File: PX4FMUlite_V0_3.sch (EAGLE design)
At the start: 145 parts, among them J2 DF13-4P-1.25V, J201 DF13C-6P-1.25V, J202 DF13C-6P-1.25V, J203 DF13C-6P-1.25V, J301 47346-0001, J302 DF13C-4P-1.25V, J401 DF13C-4P-1.25V, J403 DF13C-7P-1.25V, J405 DF13C-4P-1.25V, J801 JST-ZH-3, J802 DF13C-3P-1.25V, M3_MOUNT1101 MOUNT-HOLE3.1MM, M3_MOUNT1102 MOUNT-HOLE3.1MM, M3_MOUNT1103 MOUNT-HOLE3.1MM, M3_MOUNT1104 MOUNT-HOLE3.1MM, U1 MPU-6000QFN-24, U101 STM32F4X7VX, U401 MAX3051, U903 74LVC2G240, X101 3.2x2.5 mm / 24 MHz / 15 ppm

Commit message: More tweaks
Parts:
- removed J301: 47346-0001, pixhawk2:MOLEX-47346-0001
- removed R12, R13: 120R, pixhawk2:RESISTOR0402-RES
- removed U$301: NUF2042XV6, pixhawk2:NUF2042XV6
- added C4: 0u1, pixhawk2:CAP0402
- added J3: DF13C-4P-1.25V, con-hirose-df13:DF13-4P-1.25V
- added JP3: JUMPER-3SMD, SparkFun-Passives:JUMPER-3SMD
- added L7: KNH16C104DA5TS, pixhawk2:KNH16C104DA5TS
- added R4: 120R, pixhawk2:RESISTOR0402-RES
- added SJ2: SOLDERJUMPERTRACE, SparkFun-Passives:SOLDERJUMPERTRACE
- added U$5: NUF2042XV6, PX4lite:NUF2042XV6
- added U$7: PESD0402-140, pixhawk2:DIODE-TVS
- added U2: MAX3051, pixhawk2:MAX3051MAX3051EKA
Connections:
- removed net N$14: J203.4, R12.2
- removed net N$19: J203.5, R13.2
- new net N$28: J3.1, L7.P$2, U$7.C
- new net N$29: R4.2, SJ2.1
- new net N$31: JP3.2, L4.P$1
- net CAN2_RX: now also U2.DOUT; no longer R13.1
- net CAN2_TX: now also U2.DIN; no longer R12.1
- net CAN_H: now also J3.2, R4.1, U2.CANH
- net CAN_L: now also J3.3, SJ2.2, U2.CANL
- net FMU-VDD_3V3: now also C4.1, U2.VCC
- net GND: now also L6G$9.GND
- net GNDX: now also C4.2, J3.4, L7.P$3, U$5.GND, U$7.A, U2.GND, U2.RS, U2.SHDN; no longer J301.5, J301.GND1, J301.GND2, J301.GND3, J301.GND4, U$301.GND
- net OTG_DM1: now also U$5.D2I; no longer J301.2, U$301.D1I
- net OTG_DP1: now also U$5.D1I; no longer J301.3, U$301.D2I
- net OTG_FS_DM: now also U$5.D2O; no longer U$301.D1O
- net OTG_FS_DP: now also U$5.D1O; no longer U$301.D2O
- net VBUS: now also U$5.VBUS; no longer J301.1, U$301.VBUS
- net VDD_5V_PERIPH: now also JP3.1, JP3.3, L5.P$1, L7.P$1
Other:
- moved on the sheet: C2, C3, C402, J2, J302, J401, J405, L4, L403, L5, L6G$1, L6G$2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

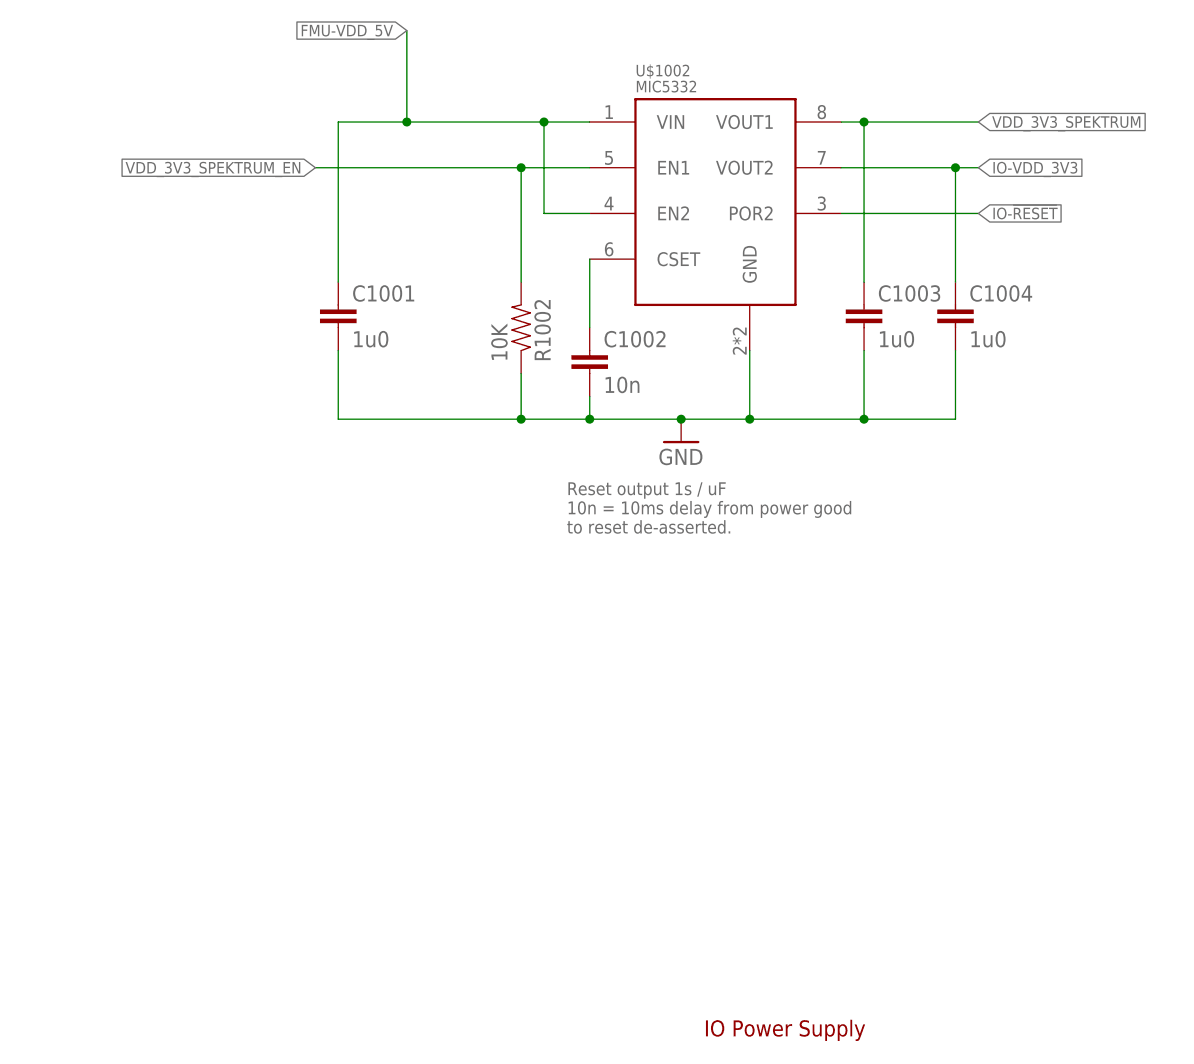
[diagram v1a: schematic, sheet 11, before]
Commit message: Change IO power to 3V3 peripheral power
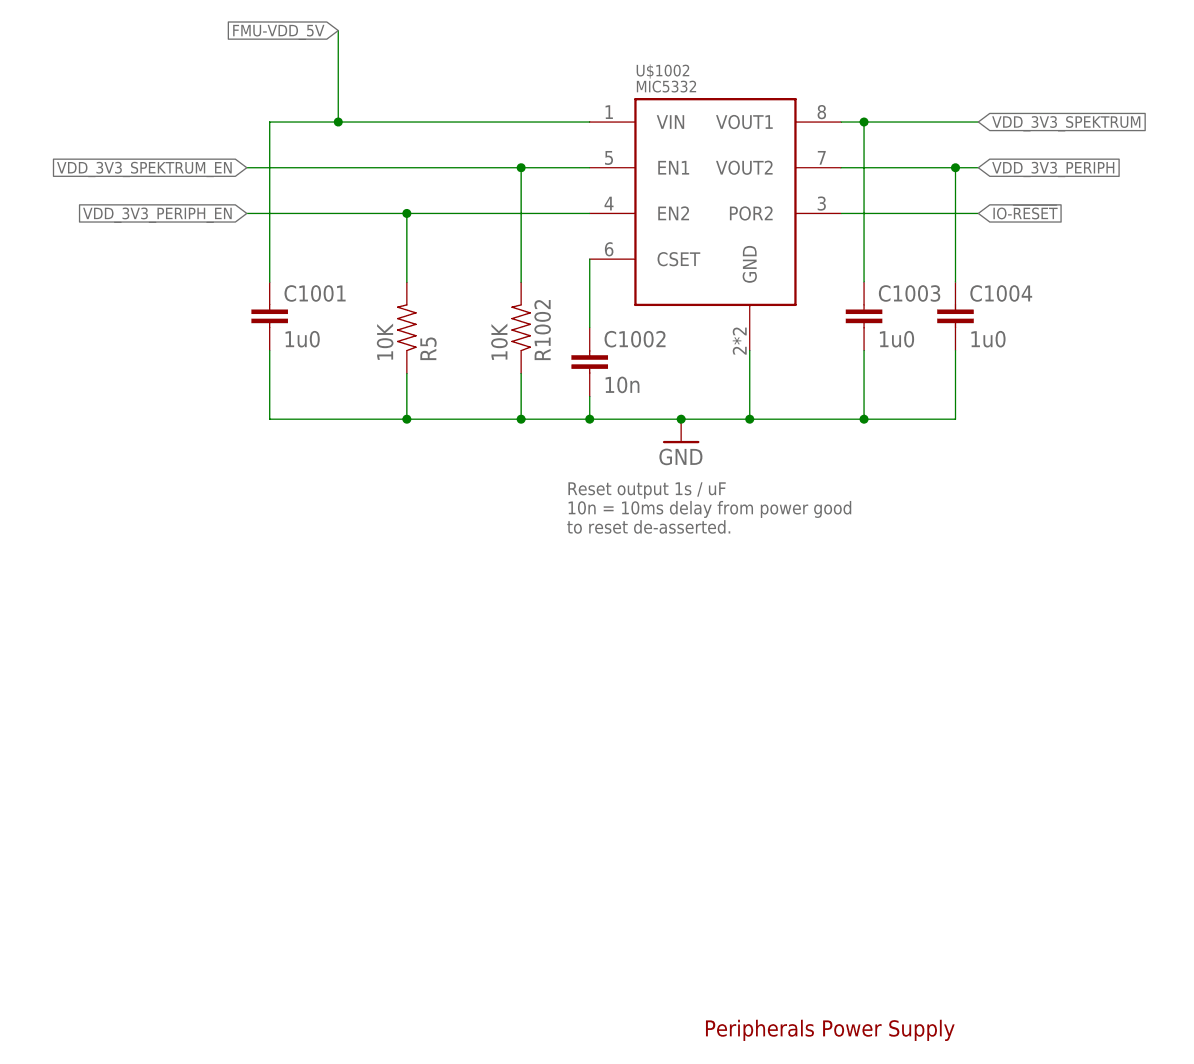
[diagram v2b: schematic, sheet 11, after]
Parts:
- removed ADC_PR, IO-BOOT1101, VDD_5V_BRICK: PAD.04, pixhawk2:PAD.04
- added R5: 10K, pixhawk2:RESISTOR0402-RES
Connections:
- removed net CAN_H: CAN_H.P$1, J3.2, J405.2, R4.1, R409.1, U2.CANH, U401.CANH
- removed net CAN_L: CAN_L.P$1, J3.3, J405.3, SJ1.2, SJ2.2, U2.CANL, U401.CANL
- removed net IO-BOOT0: IO-BOOT1101.P$1
- removed net IO-VDD_3V3: C1004.1, C901.1, U$1002.VOUT2, U903.VCC
- removed net PRESSURE_SENS_IN: ADC_PR.P$1
- removed net VDD_5V_BRICK: VDD_5V_BRICK.P$1
- new net CAN1_H: CAN_H.P$1, J405.2, R409.1, U401.CANH
- new net CAN1_L: CAN_L.P$1, J405.3, SJ1.2, U401.CANL
- new net CAN2_H: J3.2, R4.1, U2.CANH
- new net CAN2_L: J3.3, SJ2.2, U2.CANL
- new net VDD_3V3_PERIPH: C1004.1, C901.1, JP3.1, U$1002.VOUT2, U903.VCC
- new net VDD_3V3_PERIPH_EN: R5.2, U$1002.EN2
- net FMU-BOOT0: no longer FMU-BOOT1101.P$1
- net FMU-VDD_5V: no longer U$1002.EN2
- net GNDX: now also R5.1
- net VDD_5V_PERIPH: no longer JP3.1
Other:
- note added: "Peripherals Power Supply"
- note removed: "IO Power Supply"
- moved on the sheet: C1001

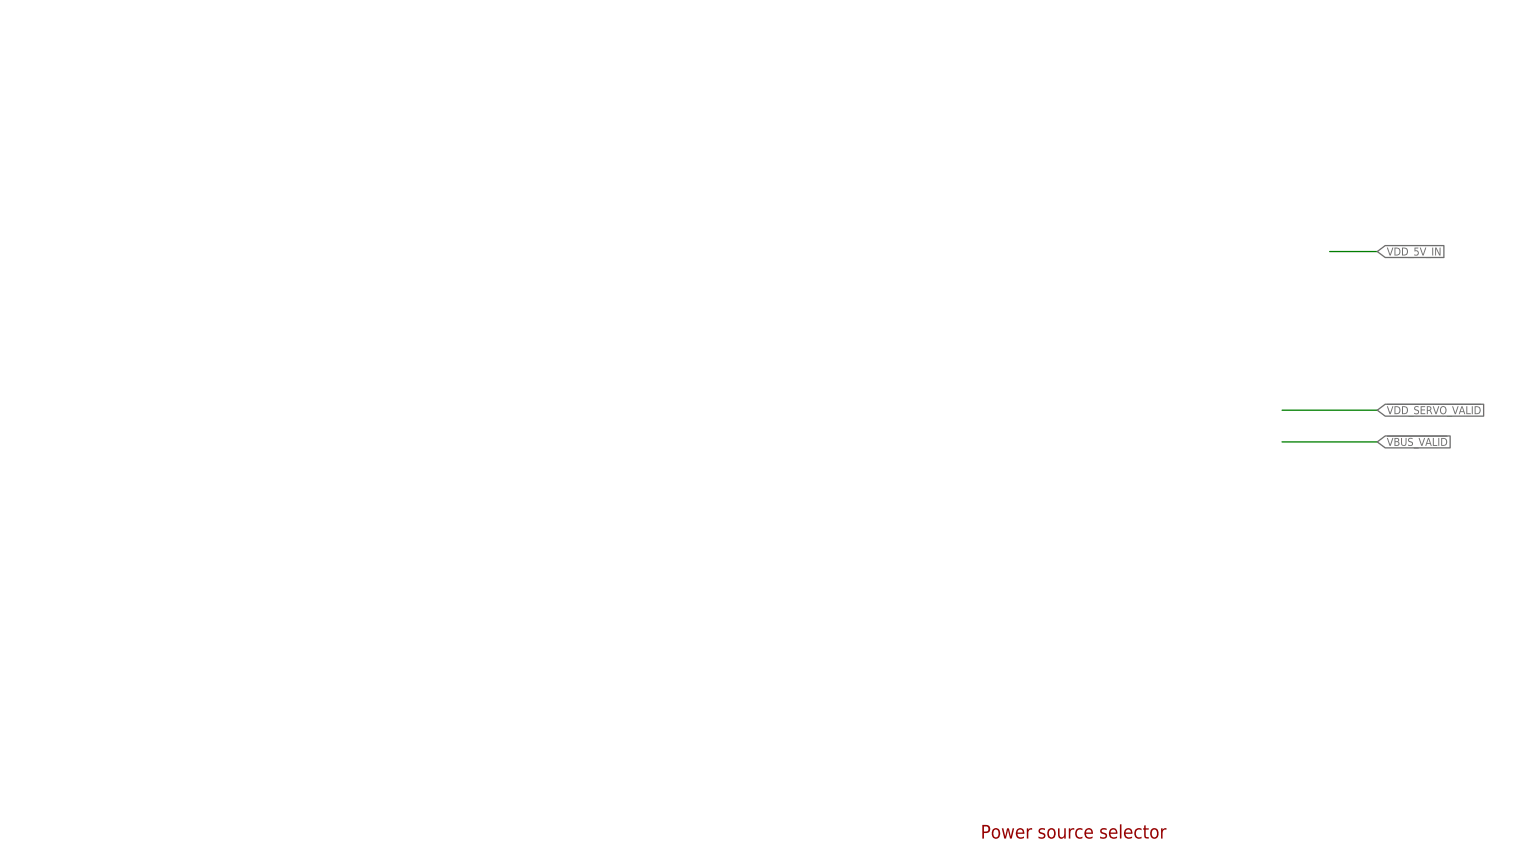
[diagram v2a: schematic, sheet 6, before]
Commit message: Added TPS62143 buck, moved mounting points
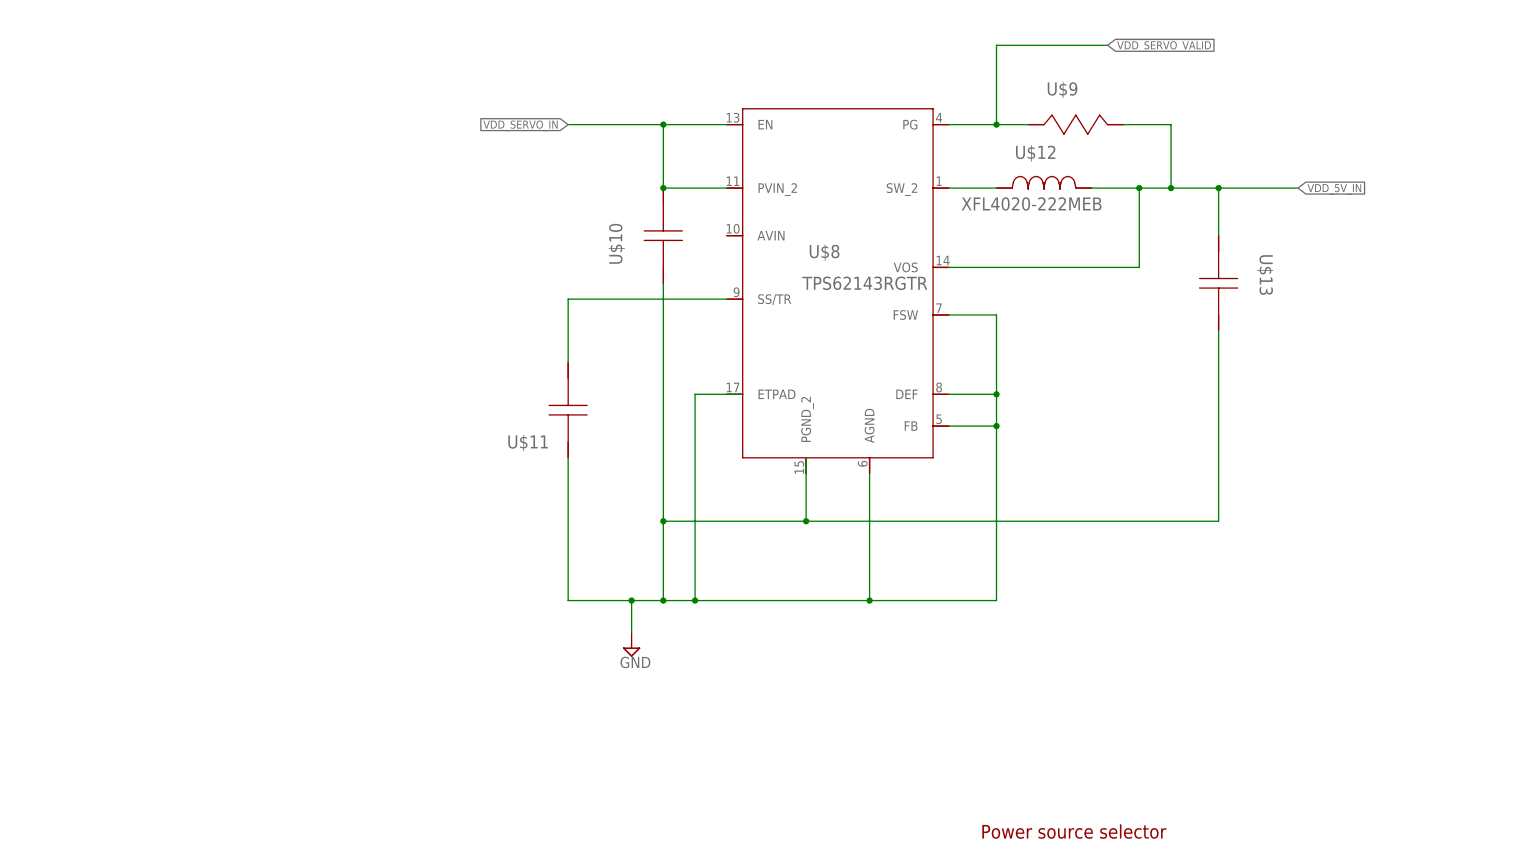
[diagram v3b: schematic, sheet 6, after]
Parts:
- added U$10: GRM21BR61C106KE15L, ti_tps_soln2:GRM21BR61C106KE15L
- added U$11: GRM155R61C223KA01D, ti_tps_soln2:GRM155R61C223KA01D
- added U$12: XFL4020-222MEB, ti_tps_soln2:XFL4020-222MEB
- added U$13: LMK212BJ226MG-T, ti_tps_soln2:LMK212BJ226MG-T
- added U$8: TPS62143RGTR, ti_tps_soln2:TPS62143RGTR
- added U$9: CRCW0402100KFKED, ti_tps_soln2:CRCW0402100KFKED
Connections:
- new net N$14: U$12.2, U$8.SW_2
- new net N$40: U$11.1, U$8.SS/TR
- net !VDD_SERVO_VALID: now also U$8.PG, U$9.2
- net GND: now also U$10.2, U$11.2, U$13.1, U$8.AGND, U$8.DEF, U$8.ETPAD, U$8.FB, U$8.FSW, U$8.PGND_2
- net VDD_5V_IN: now also U$12.1, U$13.2, U$8.VOS, U$9.1
- net VDD_SERVO_IN: now also U$10.1, U$8.EN, U$8.PVIN_2
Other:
- moved on the sheet: JX301-GND1, JX301-GND2, JX301-GND3, JX301-TCK/SWCLK, JX301-TDI/EXTB, JX301-TDO/SWO, JX301-TMS/SWDIO, JX301-VTREF, JX301-~{RESET}

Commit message: Changed to MAX21100
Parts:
- removed C1: 10n, pixhawk2:CAP0402
- removed C507: 0u1, pixhawk2:CAP0402
- removed C509: 10u/10V, pixhawk2:CAP0805
- removed C510: 0u47, pixhawk2:CAP0402
- removed S4RX, S4TX, S5_RX, S5_TX: PAD.04, pixhawk2:PAD.04
- removed U1: MPU-6000QFN-24, SparkFun-Sensors:MPU-6000QFN-24
- added C5: 0u1, pixhawk2:CAP0402
- U$2: value LSM303D -> MAX21100; device PX4FMUlite_V0_1:LSM303D -> PX4lite:MAX21100
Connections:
- removed net N$10: C510.1, U$2.SETC
- removed net N$17: C510.2, U$2.SETP
- removed net N$25: C505.1, U1.CPOUT
- removed net N$27: C1.1, U1.REGOUT
- removed net N$6: C509.1, U$2.C1
- removed net SERIAL4_RX: L3G$3.P$2, S4RX.P$1
- removed net SERIAL4_TX: L3G$4.P$2, S4TX.P$1
- removed net SERIAL5_RX: L3G$1.P$2, S5_RX.P$1
- removed net SERIAL5_TX: L3G$2.P$2, S5_TX.P$1
- new net REGD: C5.1, U$2.REGD
- net !ACCEL_MAG_CS: no longer U$2.CS
- net !GYRO_CS: now also U$2.CS; no longer U1.CS
- net FMU-UART7_RX: no longer L3G$1.P$1
- net FMU-UART7_TX: no longer L3G$2.P$1
- net FMU-UART8_RX: no longer L3G$3.P$1
- net FMU-UART8_TX: no longer L3G$4.P$1
- net GND: no longer C1.2
- net GNDX: now also C5.2, U$2.GND, U$2.RSV1; no longer C507.2, C509.2, U$2.GND@1, U$2.GND@2, U$2.GND@3, U$2.GND@4, U$2.RSRV, U1.CLKIN, U1.FSYNC, U1.GND
- net GYRO_DRDY: no longer U1.INT
- net MAG_DRDY: no longer U$2.INT2
- net SPI_INT_MISO: now also U$2.SA0/MISO; no longer U$2.SDO/SA0, U1.AD0/SDO
- net SPI_INT_MOSI: now also U$2.SDA/MOSI; no longer U$2.SDA/SDI/SDO, U1.SDA/SDI
- net SPI_INT_SCK: now also U$2.SCL/CLK; no longer U$2.SCL/SPC, U1.SCL/SCLK
- net VDD_3V3_SENSORS: now also C505.1, U$2.RSV2; no longer C507.1, U1.VDD
- net VDD_SERVO_IN: now also U$8.AVIN
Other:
- note removed: "THIS IS A SPARKFUN LIBRARY PART USED FOR REFERENCE ONLY. MUST BE REPLACED WITH OWN LIBRARY PART"
- moved on the sheet: C505, C506, C508, U$10
